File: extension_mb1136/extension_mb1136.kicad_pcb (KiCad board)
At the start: 2 copper layers, 70 x 57.5 mm, 31 parts, among them CN1 Conn_02x19_Odd_Even, CN2 Conn_02x19_Odd_Even, CN3 Conn_01x08, CN4 Conn_01x06, CN5 Conn_01x08, CN6 Conn_01x10, J1 Conn_01x03, J2 Conn_01x03, Q1 S9013, SW1 USB_SEL, SW2 USB_SEL, U1 STMPS2151MTR, U2 USBLC6-2

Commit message: update pcb
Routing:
- net PB12: vias 3 -> 2

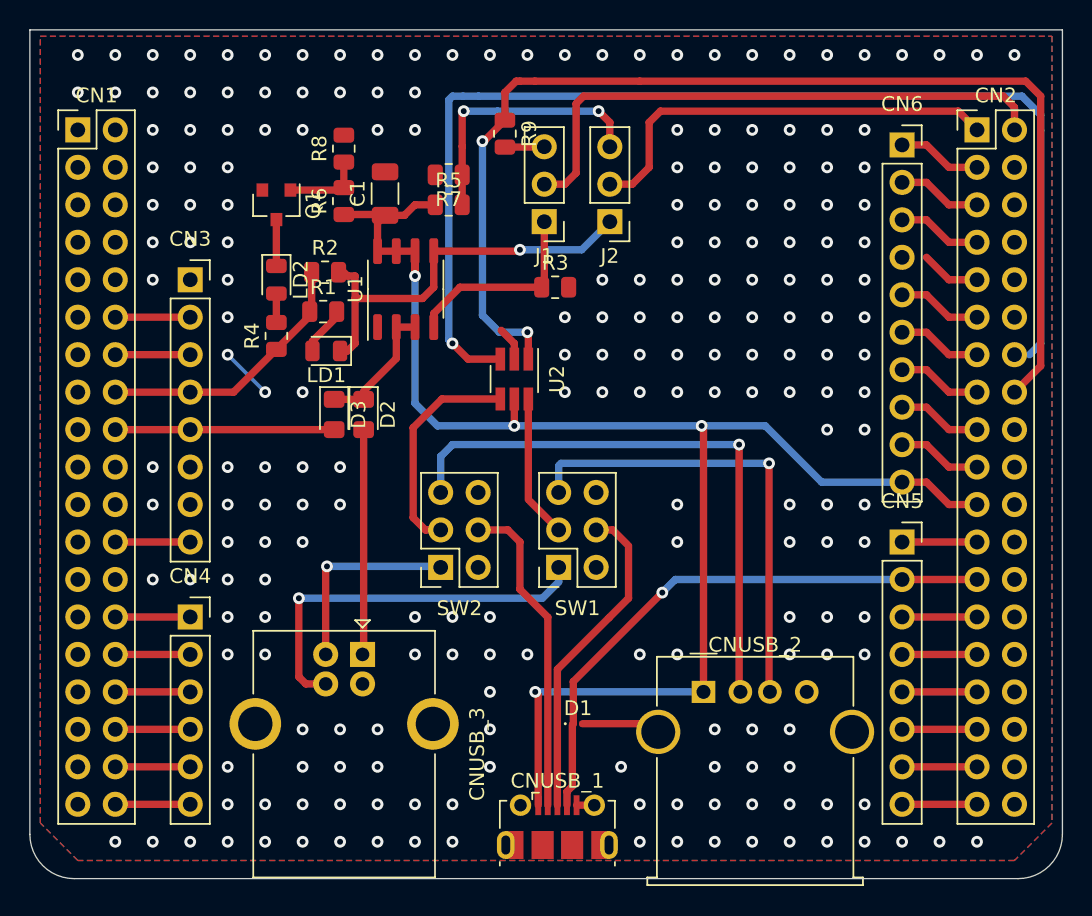
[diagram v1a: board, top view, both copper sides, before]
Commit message: change footprint for D2,D3
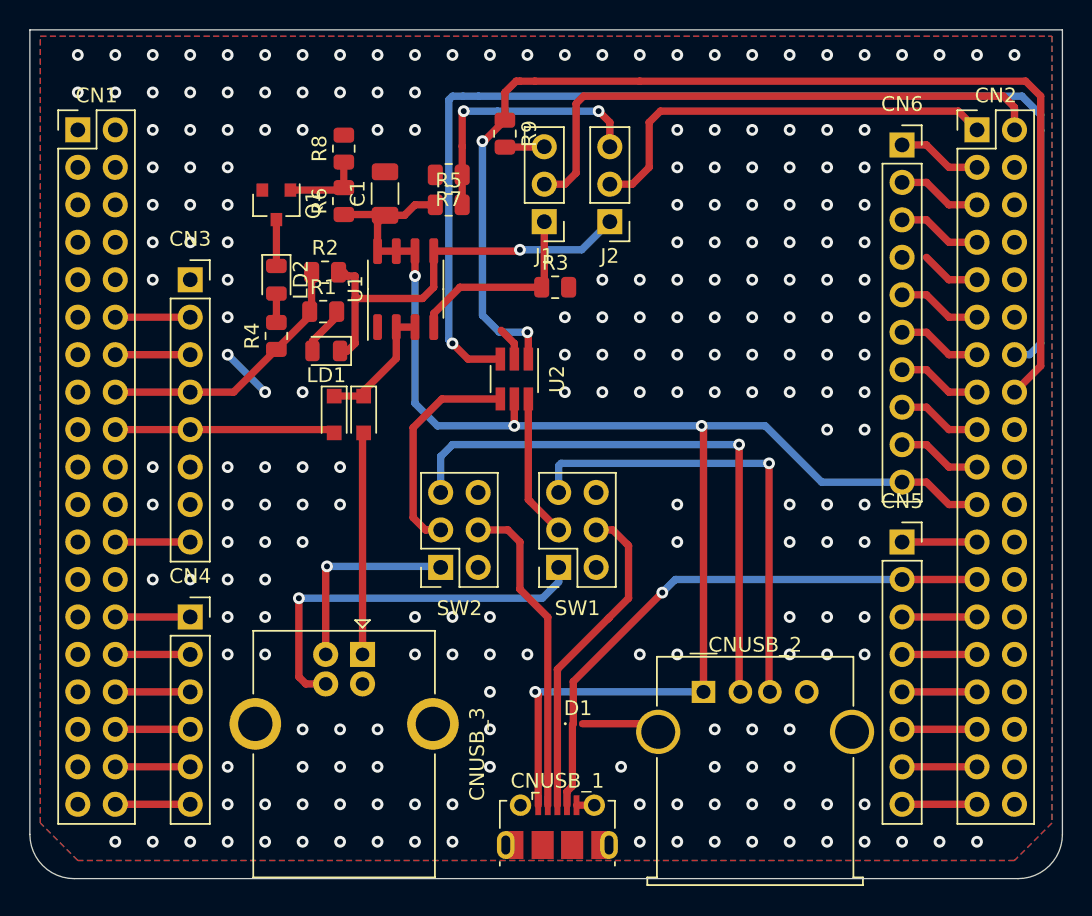
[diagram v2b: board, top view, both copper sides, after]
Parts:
- D2, D3: footprint Diode_SMD:D_0805_2012Metric_Pad1.15x1.40mm_HandSolder -> Diode_SMD:D_SOD-323_HandSoldering

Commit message: update pcb
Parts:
- D2, D3: value D -> 1N4001
- SW1, SW2: footprint Connector_PinSocket_2.54mm:PinSocket_2x03_P2.54mm_Vertical -> Connector_PinHeader_2.54mm:PinHeader_2x03_P2.54mm_Vertical
- moved CNUSB_2 1.27 mm to (66.5, 91.4)
- moved CNUSB_1 1.03 mm to (56.9, 100.6)
- moved R2 0.76 mm to (42.2, 62.2)
- moved D1 0.13 mm to (59.3, 93.5)
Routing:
- net Net-(CNUSB_1-Pad2): track 21.8 -> 26.9 mm
- net GND: track 16.5 -> 20.6 mm
- net Net-(SW2-Pad3): track 15.0 -> 11.5 mm
- net PB10: track 38.7 -> 41.2 mm
- net Net-(SW1-Pad3): track 9.73 -> 12.1 mm
- net Net-(CNUSB_3-Pad2): track 13.7 -> 12.0 mm
- net Net-(CNUSB_2-Pad2): track 39.8 -> 38.3 mm
- net Net-(CNUSB_1-Pad3): track 22.3 -> 21.0 mm
- net Net-(CNUSB_2-Pad3): track 31.7 -> 30.6 mm
- net Net-(CNUSB_3-Pad3): track 26.4 -> 25.4 mm
- net +3V3: track 18.5 -> 19.3 mm
